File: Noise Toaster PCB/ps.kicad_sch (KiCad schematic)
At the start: 8 parts

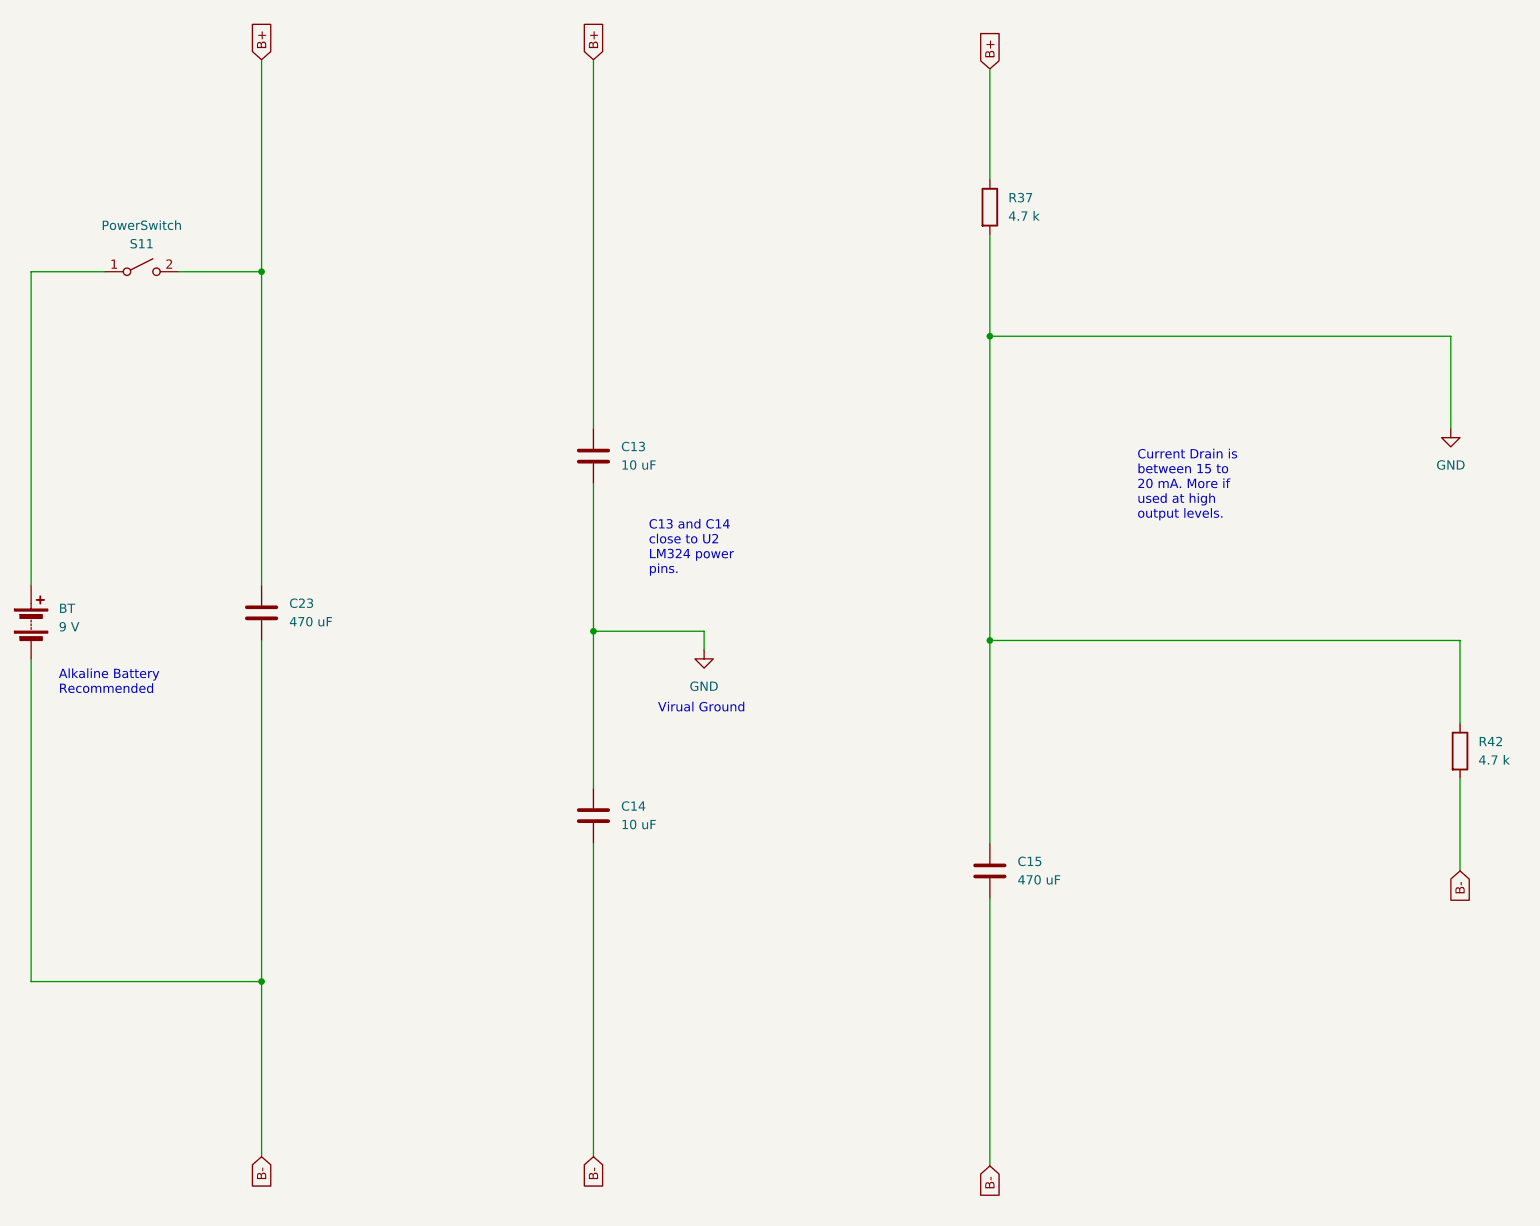
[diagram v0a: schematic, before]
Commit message: updated schematics
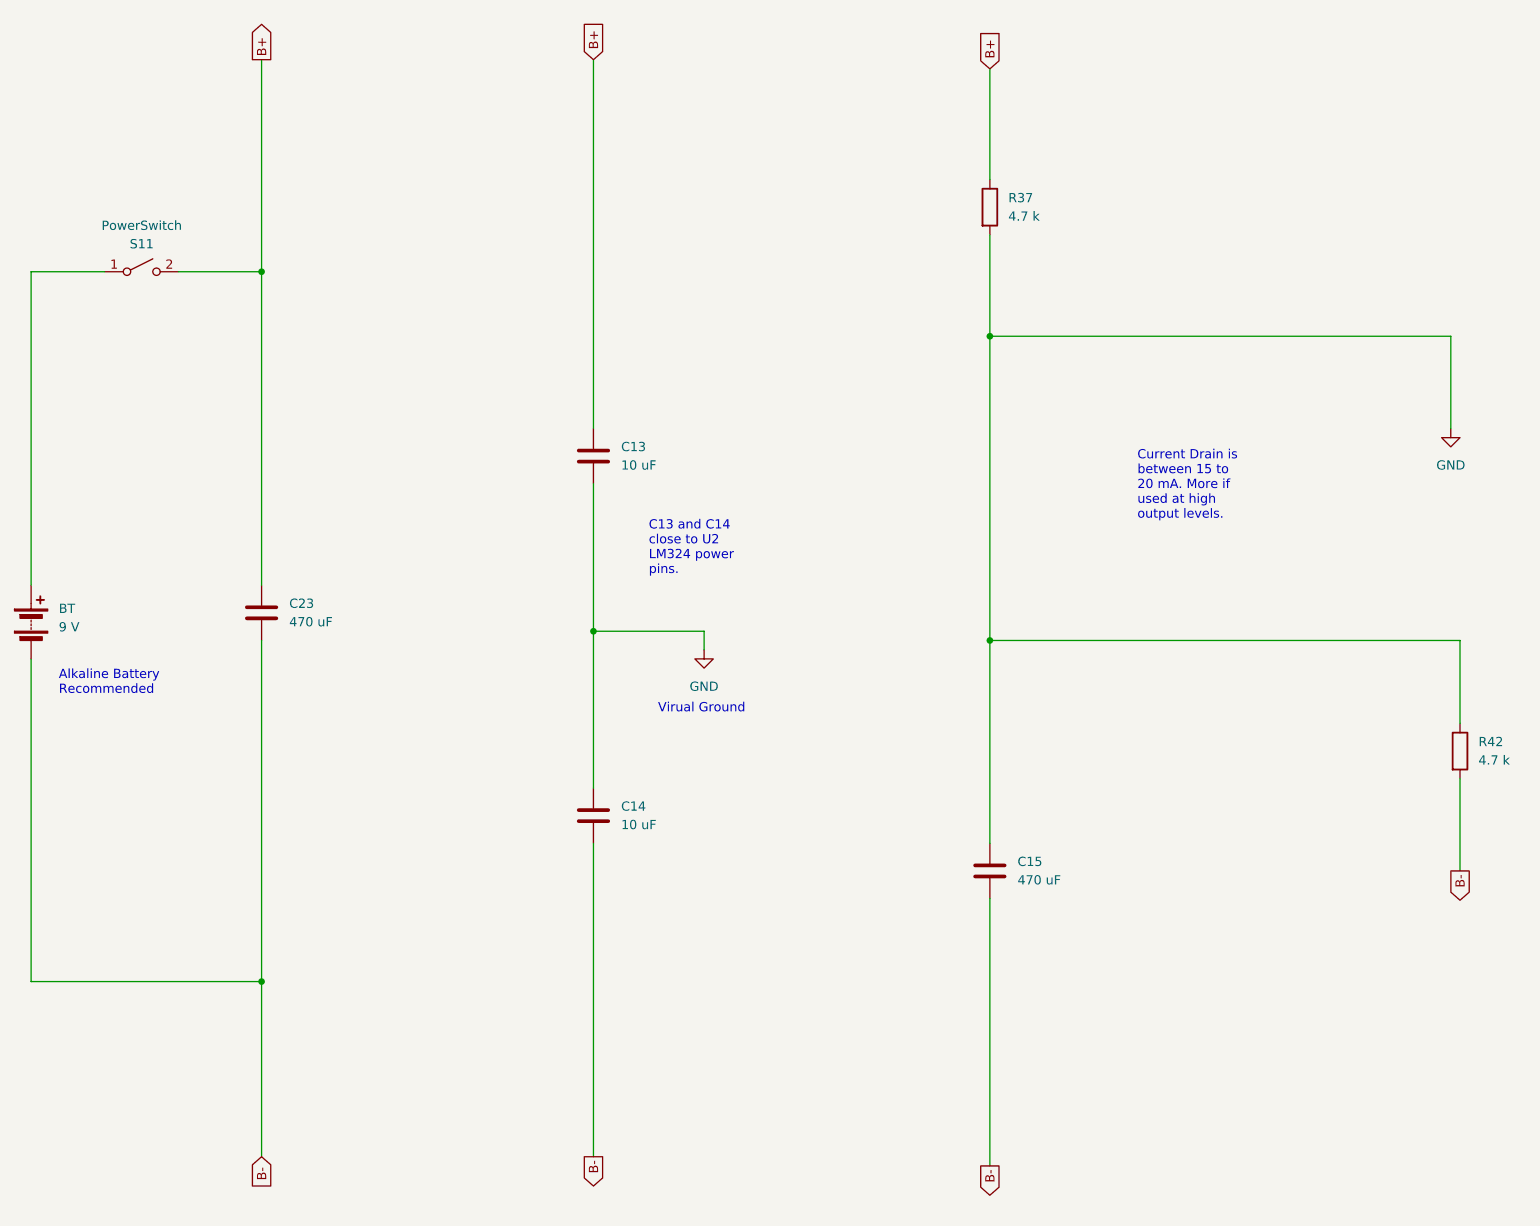
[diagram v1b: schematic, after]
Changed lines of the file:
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@@
     (effects (font (size 1.27 1.27)) (justify left bottom))
   )
-  (global_label "B-" (shape input) (at 160.02 177.8 270) (fields_autoplaced)
+  (global_label "B-" (shape output) (at 160.02 177.8 270) (fields_autoplaced)
     (effects (font (size 1.27 1.27)) (justify right))
     (property "Intersheetrefs" "${INTERSHEET_REFS}" (at 160.02 183.6276 90)
@@
     )
   )
-  (global_label "B-" (shape input) (at 224.79 137.16 270) (fields_autoplaced)
+  (global_label "B-" (shape output) (at 224.79 137.16 270) (fields_autoplaced)
     (effects (font (size 1.27 1.27)) (justify right))
     (property "Intersheetrefs" "${INTERSHEET_REFS}" (at 224.79 142.9876 90)
@@
     )
   )
-  (global_label "B+" (shape input) (at 59.69 25.4 90) (fields_autoplaced)
+  (global_label "B+" (shape output) (at 59.69 25.4 90) (fields_autoplaced)
     (effects (font (size 1.27 1.27)) (justify left))
     (property "Intersheetrefs" "${INTERSHEET_REFS}" (at 59.69 19.5724 90)
@@
     )
   )
-  (global_label "B-" (shape input) (at 105.41 176.53 270) (fields_autoplaced)
+  (global_label "B-" (shape output) (at 105.41 176.53 270) (fields_autoplaced)
     (effects (font (size 1.27 1.27)) (justify right))
     (property "Intersheetrefs" "${INTERSHEET_REFS}" (at 105.41 182.3576 90)
@@
     (instances
       (project "Noise Toaster PCB"
-        (path "/7be3f398-d902-4566-9ee4-0bff072cd47e/9c6b1f0b-dddb-43c5-83ba-4fcd1cf28662"
+        (path "/7be3f398-d902-4566-9ee4-0bff072cd47e/8163954c-0389-42ef-b929-449d078595e3"
           (reference "PowerSwitch") (unit 1)
         )
@@
     (instances
       (project "Noise Toaster PCB"
-        (path "/7be3f398-d902-4566-9ee4-0bff072cd47e/9c6b1f0b-dddb-43c5-83ba-4fcd1cf28662"
+        (path "/7be3f398-d902-4566-9ee4-0bff072cd47e/8163954c-0389-42ef-b929-449d078595e3"
           (reference "#PWR01") (unit 1)
         )
@@
     (instances
       (project "Noise Toaster PCB"
-        (path "/7be3f398-d902-4566-9ee4-0bff072cd47e/9c6b1f0b-dddb-43c5-83ba-4fcd1cf28662"
+        (path "/7be3f398-d902-4566-9ee4-0bff072cd47e/8163954c-0389-42ef-b929-449d078595e3"
           (reference "C13") (unit 1)
         )
@@
     (instances
       (project "Noise Toaster PCB"
-        (path "/7be3f398-d902-4566-9ee4-0bff072cd47e/9c6b1f0b-dddb-43c5-83ba-4fcd1cf28662"
+        (path "/7be3f398-d902-4566-9ee4-0bff072cd47e/8163954c-0389-42ef-b929-449d078595e3"
           (reference "R42") (unit 1)
         )
@@
     (instances
       (project "Noise Toaster PCB"
-        (path "/7be3f398-d902-4566-9ee4-0bff072cd47e/9c6b1f0b-dddb-43c5-83ba-4fcd1cf28662"
+        (path "/7be3f398-d902-4566-9ee4-0bff072cd47e/8163954c-0389-42ef-b929-449d078595e3"
           (reference "C14") (unit 1)
         )
@@
     (instances
       (project "Noise Toaster PCB"
-        (path "/7be3f398-d902-4566-9ee4-0bff072cd47e/9c6b1f0b-dddb-43c5-83ba-4fcd1cf28662"
+        (path "/7be3f398-d902-4566-9ee4-0bff072cd47e/8163954c-0389-42ef-b929-449d078595e3"
           (reference "BT") (unit 1)
         )
@@
     (instances
       (project "Noise Toaster PCB"
-        (path "/7be3f398-d902-4566-9ee4-0bff072cd47e/9c6b1f0b-dddb-43c5-83ba-4fcd1cf28662"
+        (path "/7be3f398-d902-4566-9ee4-0bff072cd47e/8163954c-0389-42ef-b929-449d078595e3"
           (reference "C23") (unit 1)
         )
@@
     (instances
       (project "Noise Toaster PCB"
-        (path "/7be3f398-d902-4566-9ee4-0bff072cd47e/9c6b1f0b-dddb-43c5-83ba-4fcd1cf28662"
+        (path "/7be3f398-d902-4566-9ee4-0bff072cd47e/8163954c-0389-42ef-b929-449d078595e3"
           (reference "C15") (unit 1)
         )
@@
     (instances
       (project "Noise Toaster PCB"
-        (path "/7be3f398-d902-4566-9ee4-0bff072cd47e/9c6b1f0b-dddb-43c5-83ba-4fcd1cf28662"
+        (path "/7be3f398-d902-4566-9ee4-0bff072cd47e/8163954c-0389-42ef-b929-449d078595e3"
           (reference "R37") (unit 1)
         )
@@
     (instances
       (project "Noise Toaster PCB"
-        (path "/7be3f398-d902-4566-9ee4-0bff072cd47e/9c6b1f0b-dddb-43c5-83ba-4fcd1cf28662"
+        (path "/7be3f398-d902-4566-9ee4-0bff072cd47e/8163954c-0389-42ef-b929-449d078595e3"
           (reference "#PWR02") (unit 1)
         )
